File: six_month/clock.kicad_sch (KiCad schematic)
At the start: 3 parts, among them U2 RV-3028-C7 32.768KHZ 1PPM TA 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

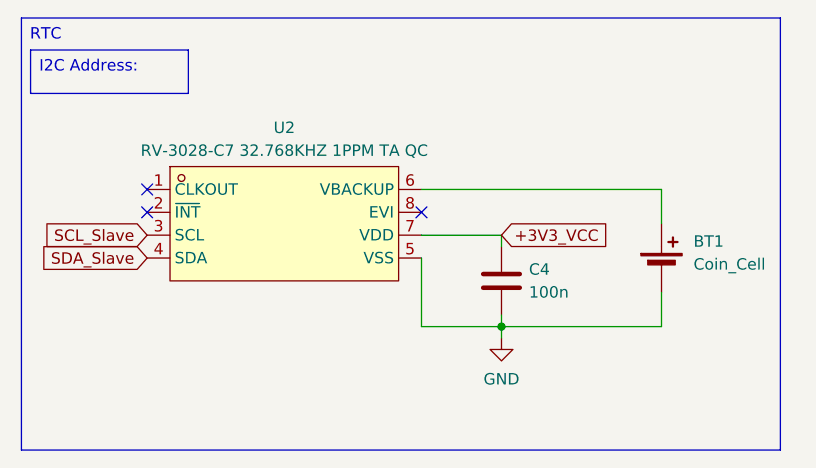
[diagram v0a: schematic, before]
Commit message: Changes
Removed the microphone idea, added a DAC for Bluetooth to Line out. Allows for external speakers to be connected via an Aux cable
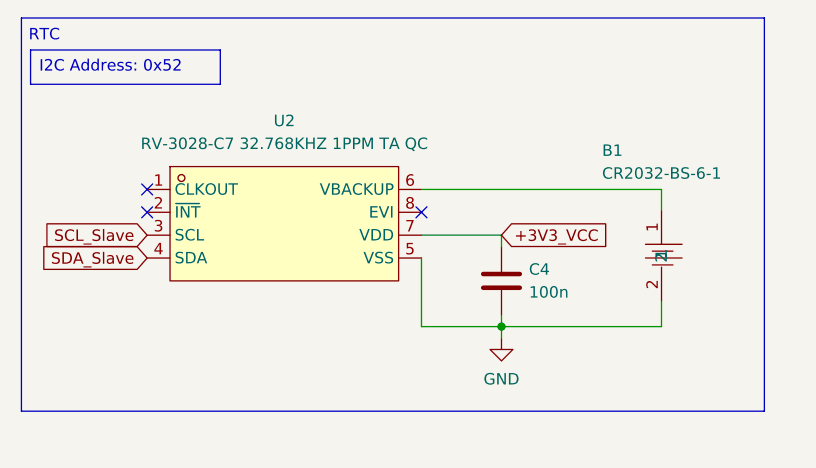
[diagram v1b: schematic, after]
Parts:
- removed BT1: Coin_Cell, Battery:Battery_Panasonic_CR2032-HFN_Horizontal_CircularHoles, symbol Device:Battery_Cell
- added B1: CR2032-BS-6-1, syms_foots:BAT-TH_CR2032-BS-6-1, symbol syms_foots:CR2032-BS-6-1
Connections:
- net GND: now also B1.2
- net at U2.6 (VBACKUP): now also B1.1
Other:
- note added: "RTC"
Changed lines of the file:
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@@
 	(generator_version "9.0")
 	(paper "A5")
-	(text_box "I2C Address: "
-		(exclude_from_sim no)
-		(at 13.716 16.256 0)
-		(size 17.526 4.826)
-		(margins 0.9525 0.9525 0.9525 0.9525)
-		(stroke
-			(width 0)
-			(type solid)
+	(rectangle
+		(start 12.7 12.7)
+		(end 95.25 56.388)
+		(stroke
+			(width 0)
+			(type default)
 		)
 		(fill
 			(type none)
 		)
+	)
+	(text "RTC"
+		(exclude_from_sim no)
+		(at 15.24 14.732 0)
 		(effects
 			(font
 				(size 1.27 1.27)
 			)
-			(justify left top)
-		)
-	)
-	(text_box "RTC"
-		(exclude_from_sim no)
-		(at 12.7 12.7 0)
-		(size 84.328 48.006)
+		)
+	)
+	(text_box "I2C Address: 0x52"
+		(exclude_from_sim no)
+		(at 13.716 16.256 0)
+		(size 21.082 3.81)
 		(margins 0.9525 0.9525 0.9525 0.9525)
 		(stroke
@@
 	(wire
 		(pts
-			(xy 83.82 46.99) (xy 83.82 43.18)
-		)
-		(stroke
-			(width 0)
-			(type default)
-		)
-	)
-	(wire
-		(pts
 			(xy 66.04 46.99) (xy 83.82 46.99)
 		)
@@
 	(wire
 		(pts
+			(xy 83.82 44.196) (xy 83.82 46.99)
+		)
+		(stroke
+			(width 0)
+			(type default)
+		)
+	)
+	(wire
+		(pts
 			(xy 66.04 36.83) (xy 66.04 38.1)
 		)
@@
 	(wire
 		(pts
-			(xy 83.82 35.56) (xy 83.82 31.75)
+			(xy 83.82 34.036) (xy 83.82 31.75)
 		)
 		(stroke
@@
 	)
 	(symbol
-		(lib_id "Device:Battery_Cell")
-		(at 83.82 40.64 0)
-		(unit 1)
-		(exclude_from_sim no)
-		(in_bom yes)
-		(on_board yes)
-		(dnp no)
-		(fields_autoplaced yes)
-		(property "Reference" "BT1"
-			(at 87.376 37.5284 0)
-			(effects
-				(font
-					(size 1.27 1.27)
-				)
-				(justify left)
-			)
-		)
-		(property "Value" "Coin_Cell"
-			(at 87.376 40.0684 0)
-			(effects
-				(font
-					(size 1.27 1.27)
-				)
-				(justify left)
-			)
-		)
-		(property "Footprint" "Battery:Battery_Panasonic_CR2032-HFN_Horizontal_CircularHoles"
-			(at 83.82 39.116 90)
-			(effects
-				(font
-					(size 1.27 1.27)
-				)
-				(hide yes)
-			)
-		)
-		(property "Datasheet" "~"
-			(at 83.82 39.116 90)
-			(effects
-				(font
-					(size 1.27 1.27)
-				)
-				(hide yes)
-			)
-		)
-		(property "Description" "Single-cell battery"
-			(at 83.82 40.64 0)
-			(effects
-				(font
-					(size 1.27 1.27)
-				)
-				(hide yes)
-			)
-		)
-		(pin "2"
-		)
-		(pin "1"
-		)
-		(instances
-			(project ""
-				(path "/760b3a53-058c-44df-84b8-d25bd41bf801/206359c9-b7b4-4f02-b040-b8d6a2904fbc"
-					(reference "BT1")
-					(unit 1)
-				)
-			)
-		)
-	)
-	(symbol
 		(lib_id "Device:C")
 		(at 66.04 41.91 0)
@@
 	)
 	(symbol
+		(lib_id "syms_foots:CR2032-BS-6-1")
+		(at 83.82 39.116 270)
+		(unit 1)
+		(exclude_from_sim no)
+		(in_bom yes)
+		(on_board yes)
+		(dnp no)
+		(property "Reference" "B1"
+			(at 77.216 27.432 90)
+			(effects
+				(font
+					(size 1.27 1.27)
+				)
+				(justify left)
+			)
+		)
+		(property "Value" "CR2032-BS-6-1"
+			(at 77.216 29.972 90)
+			(effects
+				(font
+					(size 1.27 1.27)
+				)
+				(justify left)
+			)
+		)
+		(property "Footprint" "syms_foots:BAT-TH_CR2032-BS-6-1"
+			(at 76.2 39.116 0)
+			(effects
+				(font
+					(size 1.27 1.27)
+				)
+				(hide yes)
+			)
+		)
+		(property "Datasheet" "https://lcsc.com/product-detail/Battery-Holders-Clips-Contacts_Button-battery-holder-CR2032_C70377.html"
+			(at 73.66 39.116 0)
+			(effects
+				(font
+					(size 1.27 1.27)
+				)
+				(hide yes)
+			)
+		)
+		(property "Description" ""
+			(at 83.82 39.116 0)
+			(effects
+				(font
+					(size 1.27 1.27)
+				)
+				(hide yes)
+			)
+		)
+		(property "LCSC Part" "C70377"
+			(at 71.12 39.116 0)
+			(effects
+				(font
+					(size 1.27 1.27)
+				)
+				(hide yes)
+			)
+		)
+		(pin "1"
+		)
+		(pin "2"
+		)
+		(instances
+			(project ""
+				(path "/760b3a53-058c-44df-84b8-d25bd41bf801/206359c9-b7b4-4f02-b040-b8d6a2904fbc"
+					(reference "B1")
+					(unit 1)
+				)
+			)
+		)
+	)
+	(symbol
 		(lib_id "syms_foots:RV-3028-C732.768KHZ1PPMTAQC")
 		(at 41.91 35.56 0)
@@
 		(fields_autoplaced yes)
 		(property "Reference" "U2"
-			(at 41.91 24.892 0)
+			(at 41.91 24.13 0)
 			(effects
 				(font
@@
 		)
 		(property "Value" "RV-3028-C7 32.768KHZ 1PPM TA QC"
-			(at 41.91 27.432 0)
+			(at 41.91 26.67 0)
 			(effects
 				(font
@@
 			)
 		)
-		(property "Datasheet" ""
+		(property "Datasheet" "https://www.microcrystal.com/fileadmin/Media/Products/RTC/App.Manual/RV-3028-C7_App-Manual.pdf"
 			(at 41.91 35.56 0)
 			(effects
